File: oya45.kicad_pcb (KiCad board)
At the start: 2 copper layers, 94 parts, among them U1 ProMicro

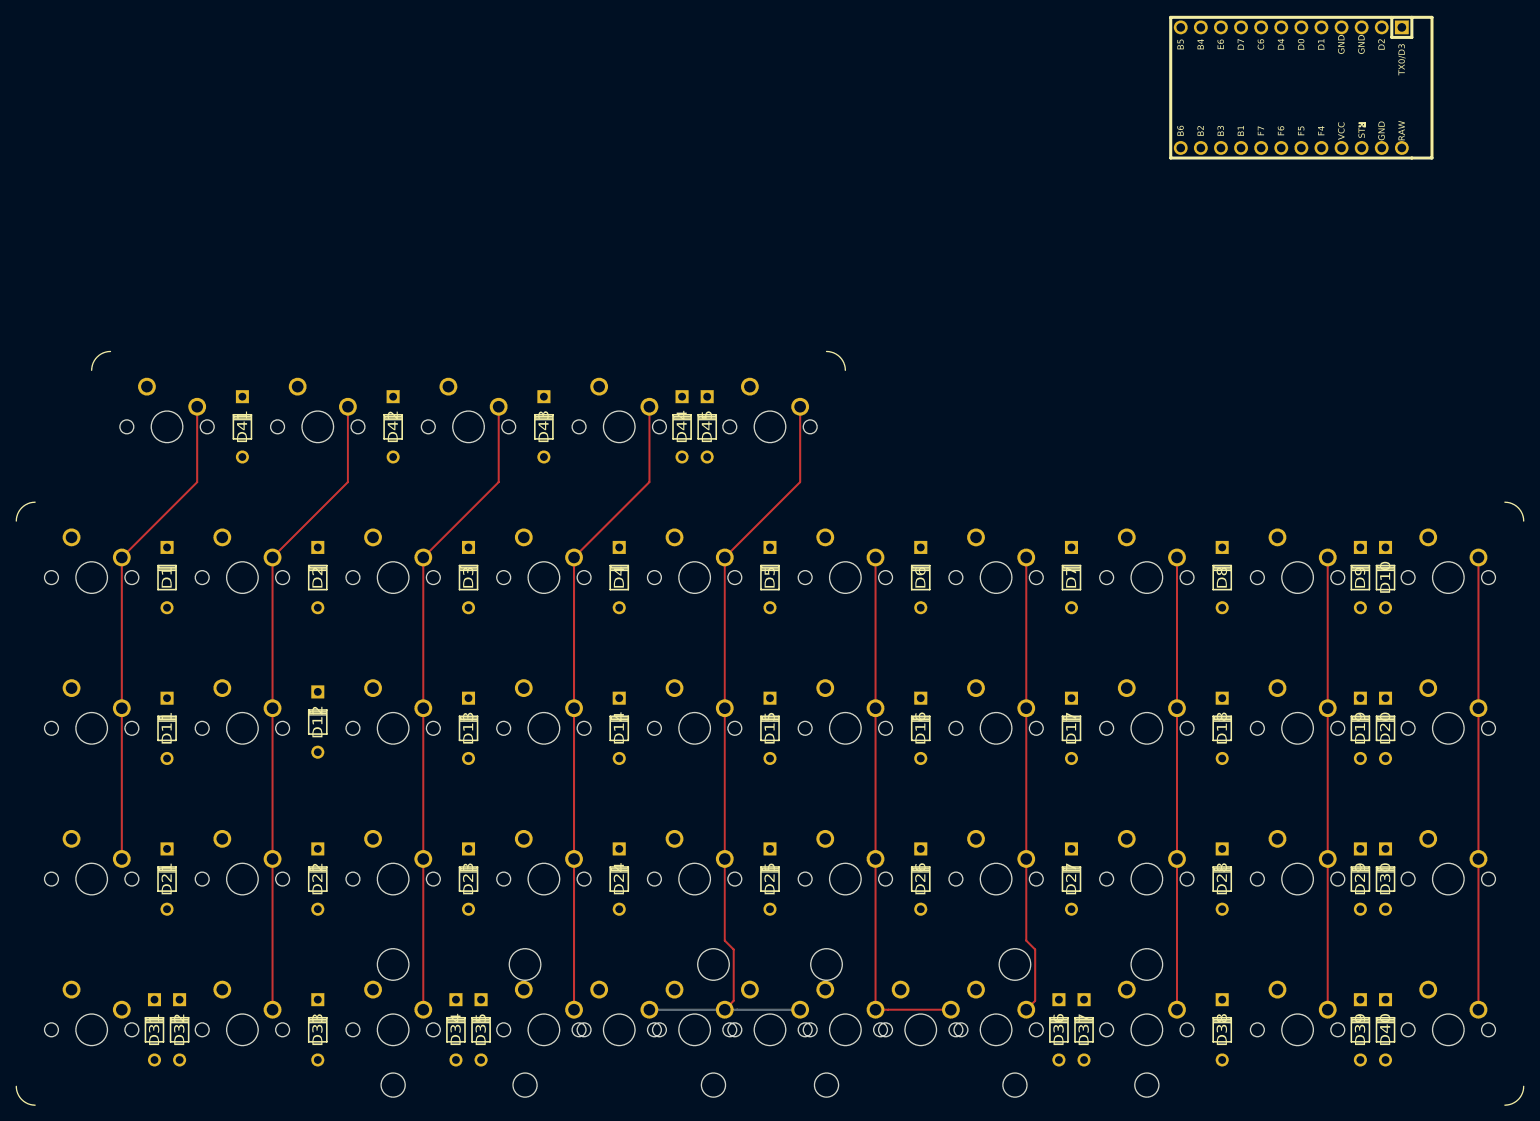
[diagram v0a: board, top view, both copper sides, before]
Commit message: column and row tracing finished
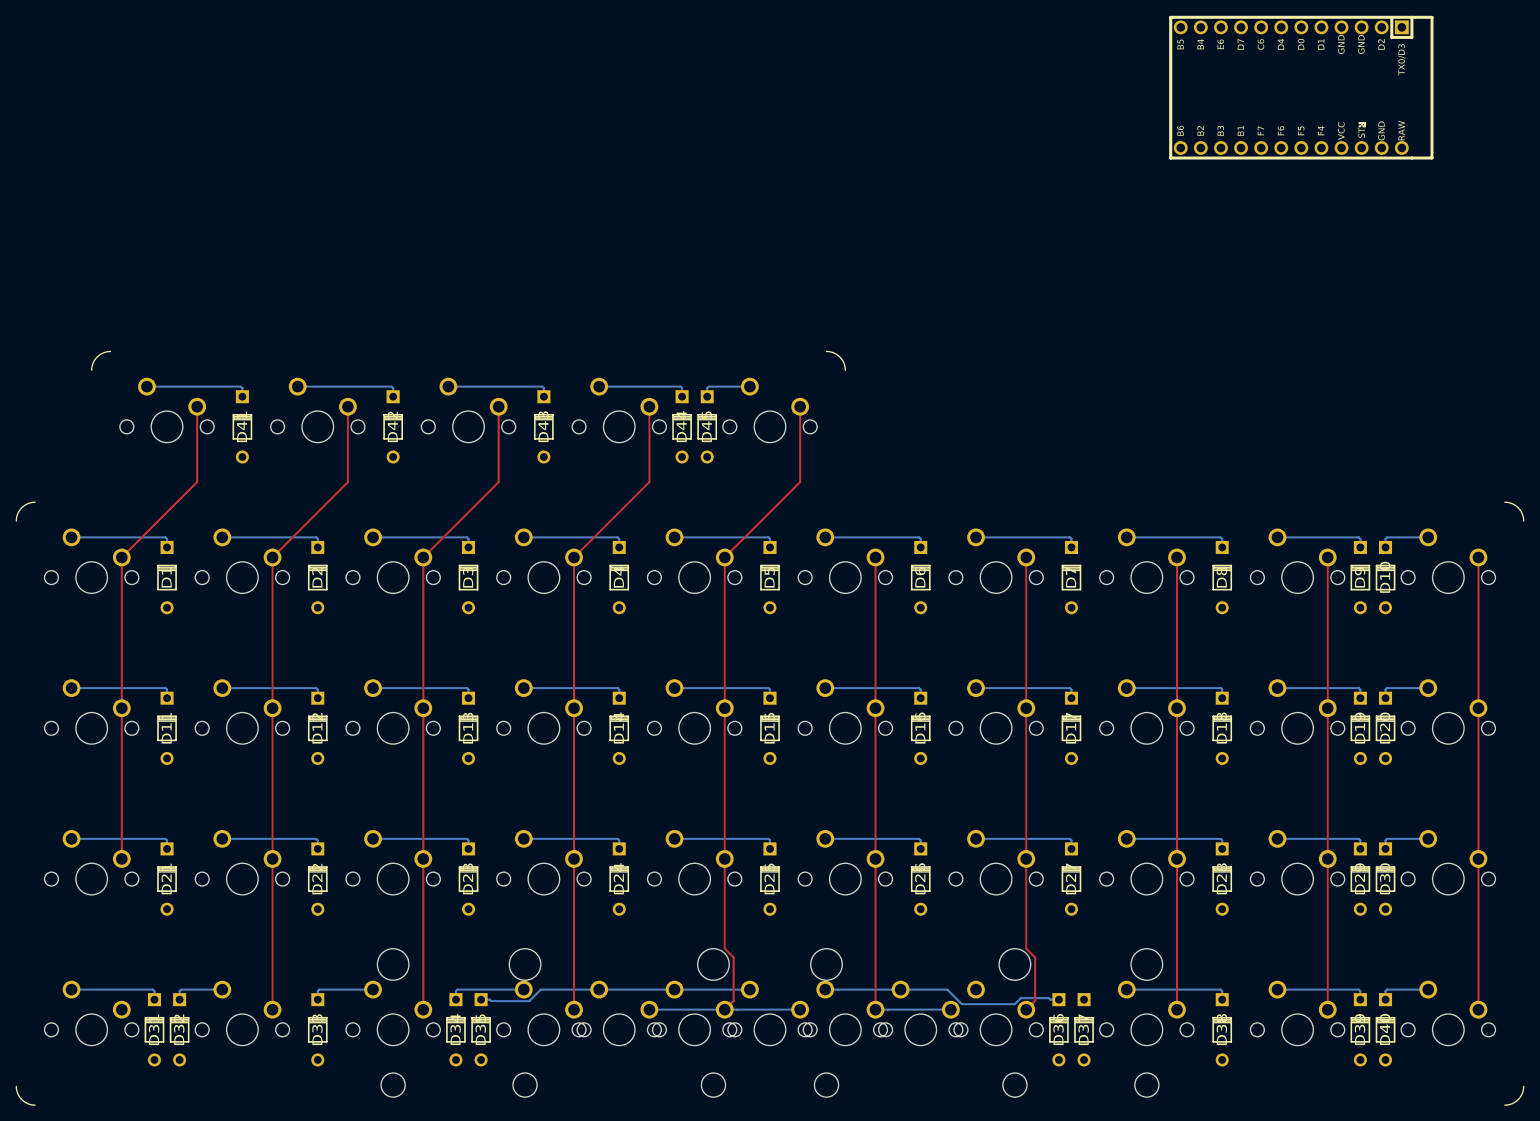
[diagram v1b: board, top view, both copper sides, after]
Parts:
- moved D12 0.79 mm to (85.7, 76.2)
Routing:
- net Net-(D35-Pad2): track 0.00 -> 34.6 mm
- net Net-(D36-Pad2): track 0.00 -> 30.7 mm
- net Net-(D3-Pad2): track 0.00 -> 13.2 mm
- net Net-(D23-Pad2): track 0.00 -> 13.2 mm
- net Net-(D13-Pad2): track 0.00 -> 13.2 mm
- net Net-(D7-Pad2): track 0.00 -> 13.2 mm
- net Net-(D5-Pad2): track 0.00 -> 13.2 mm
- net Net-(D4-Pad2): track 0.00 -> 13.2 mm
- net Net-(D2-Pad2): track 0.00 -> 13.2 mm
- net Net-(D1-Pad2): track 0.00 -> 13.2 mm
- net Net-(D8-Pad2): track 0.00 -> 13.2 mm
- net Net-(D6-Pad2): track 0.00 -> 13.2 mm
- net Net-(D27-Pad2): track 0.00 -> 13.2 mm
- net Net-(D25-Pad2): track 0.00 -> 13.2 mm
- net Net-(D17-Pad2): track 0.00 -> 13.2 mm
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
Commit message: col, row, and diode tracing finished
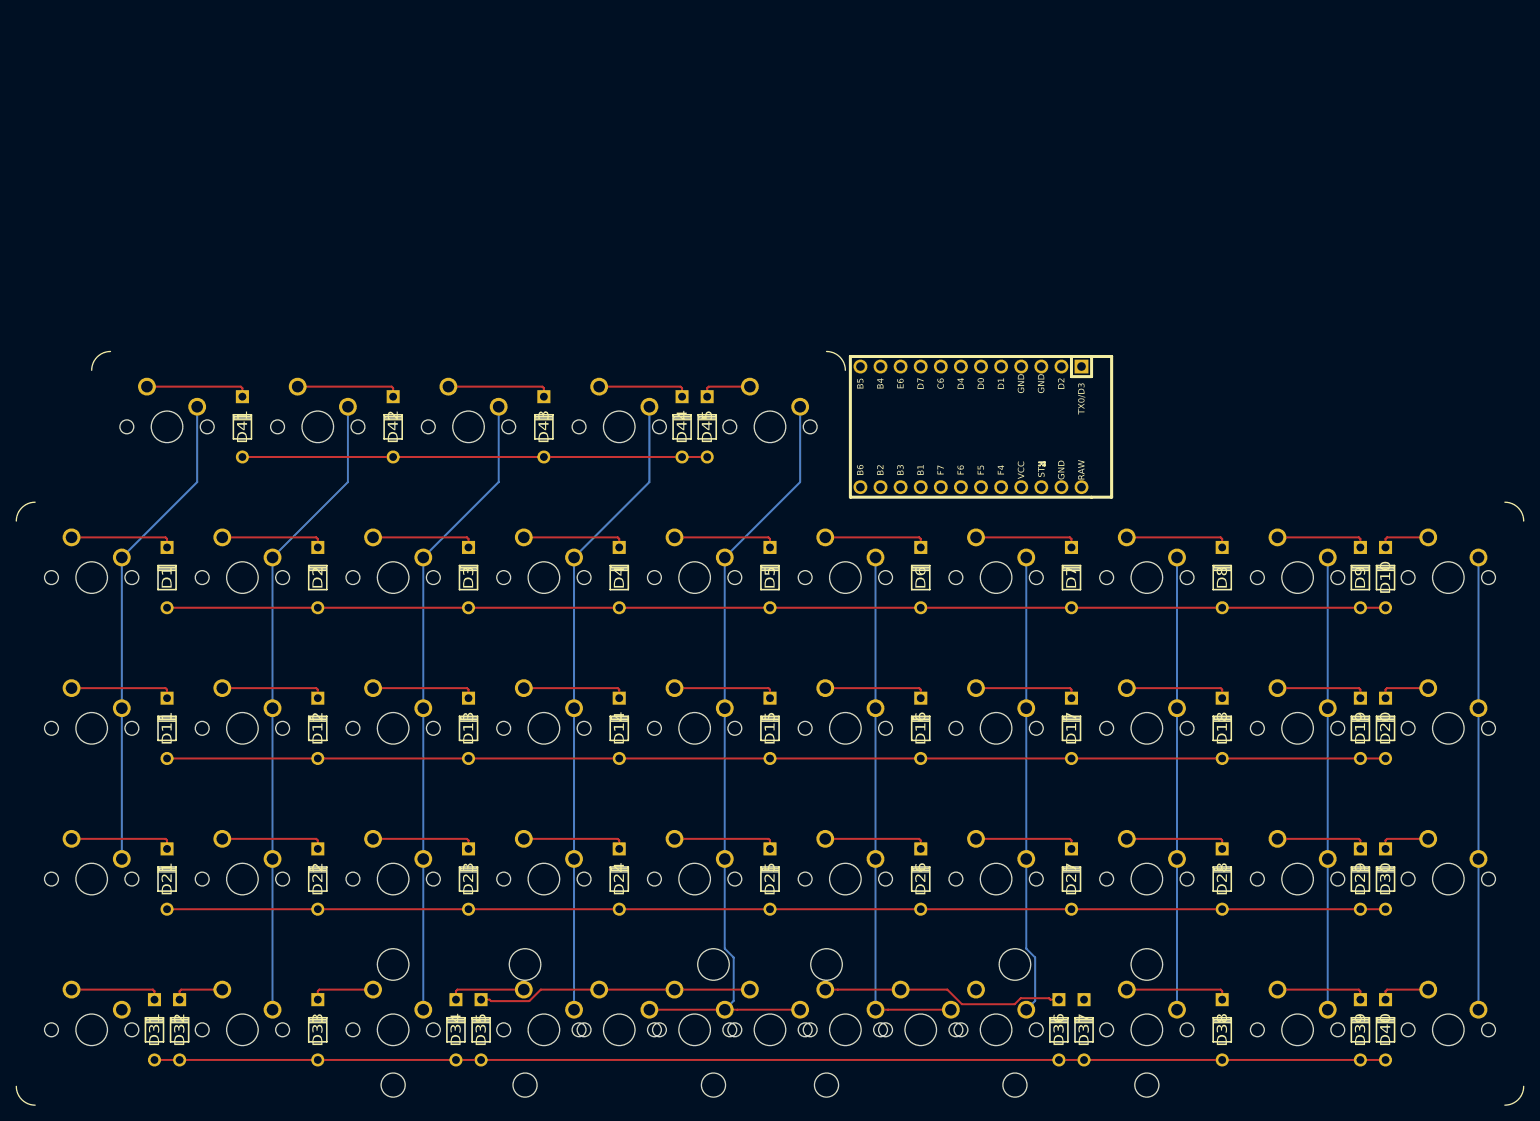
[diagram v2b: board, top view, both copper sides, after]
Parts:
- moved U1 59.0 mm to (168.3, 38.1)
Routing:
- net row4: track 0.00 -> 155.6 mm
- net row3: track 0.00 -> 154.0 mm
- net row2: track 0.00 -> 154.0 mm
- net row1: track 0.00 -> 154.0 mm
- net row0: track 0.00 -> 58.7 mm

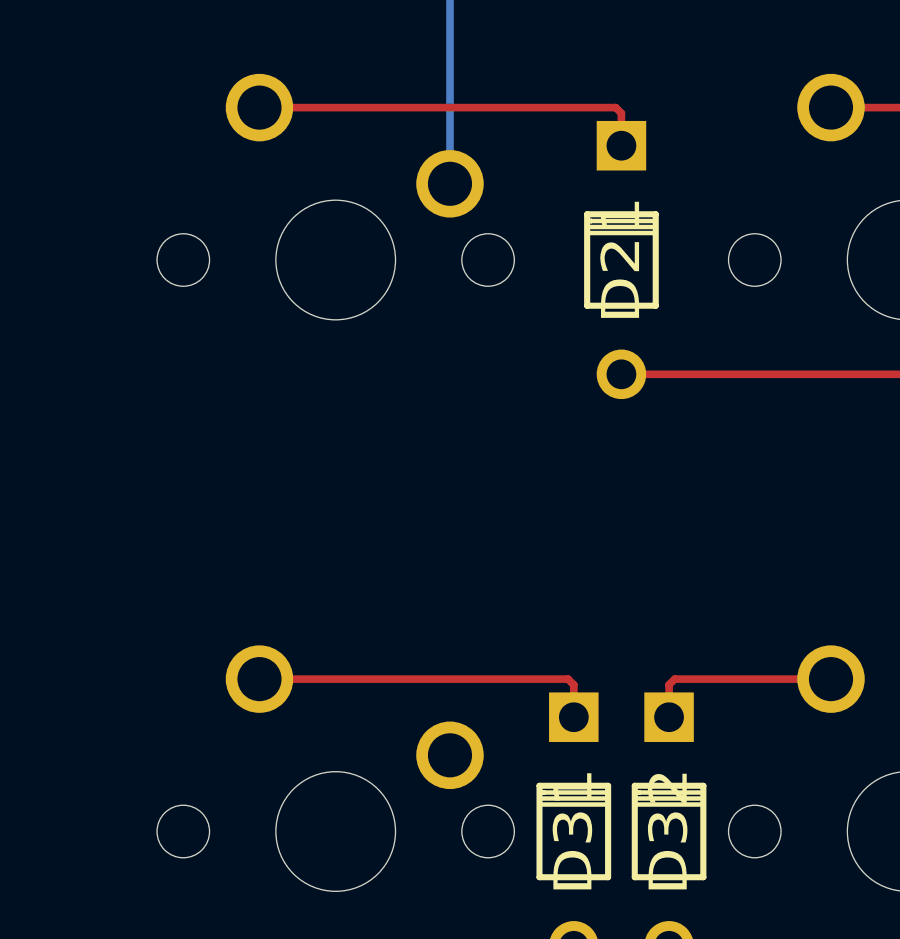
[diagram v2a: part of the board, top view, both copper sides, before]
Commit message: col, row, and diode tracing finished
fixed missing col
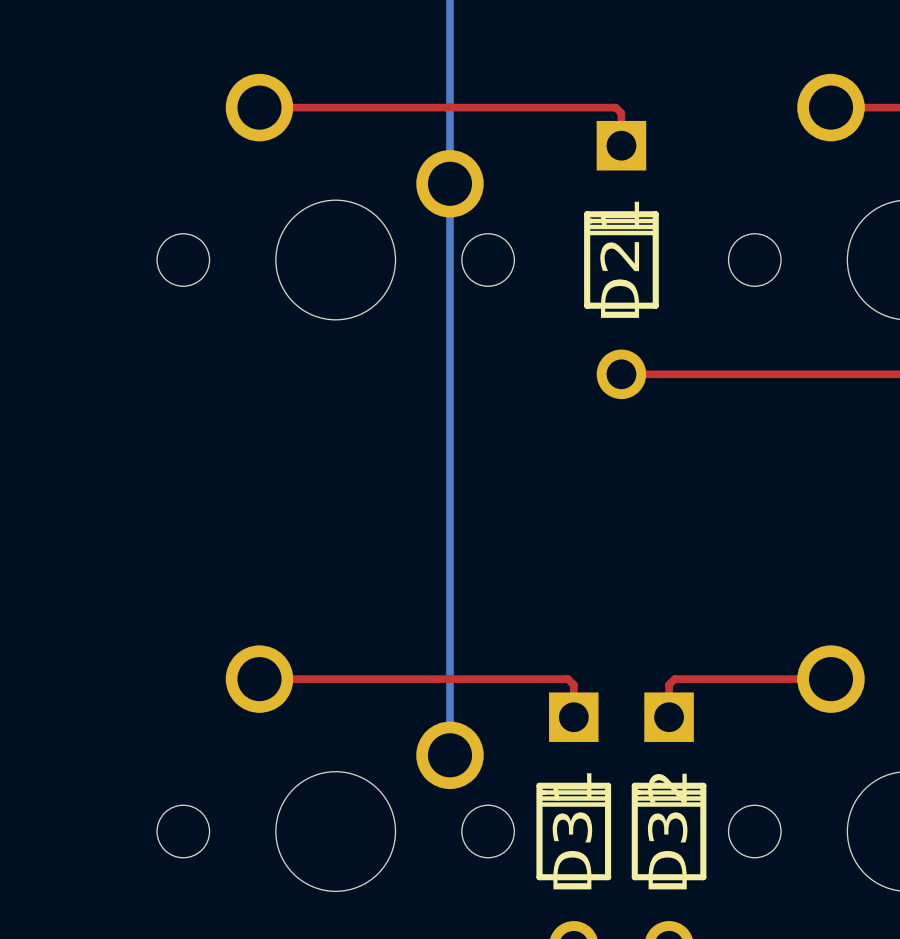
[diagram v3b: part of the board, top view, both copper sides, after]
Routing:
- net col0: track 61.1 -> 80.1 mm
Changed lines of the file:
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@@
     (thickness 1.6)
     (drawings 6)
-    (tracks 177)
+    (tracks 178)
     (zones 0)
     (modules 94)
@@
   (segment (start 70.485 35.56) (end 70.485 45.085) (width 0.254) (layer B.Cu) (net 51))
   (segment (start 60.96 54.61) (end 60.96 92.71) (width 0.254) (layer B.Cu) (net 51))
+  (segment (start 60.96 92.71) (end 60.96 111.76) (width 0.254) (layer B.Cu) (net 51))
   (segment (start 89.535 45.085) (end 80.01 54.61) (width 0.254) (layer B.Cu) (net 52))
   (segment (start 89.535 35.56) (end 89.535 45.085) (width 0.254) (layer B.Cu) (net 52))
